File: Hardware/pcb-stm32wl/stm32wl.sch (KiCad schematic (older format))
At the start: 44 parts, among them J1 S1001-46R, J2 JST-PH, J3 S1001-46R, J4 RF_Shield_One_Piece, J5 S1001-46R, J6 S1001-46R, Q1 CEN2321A, U1 TPS22917DBV, U2 TPS3839G25, U3 TPS22917DBV, U4 RP605Z283B

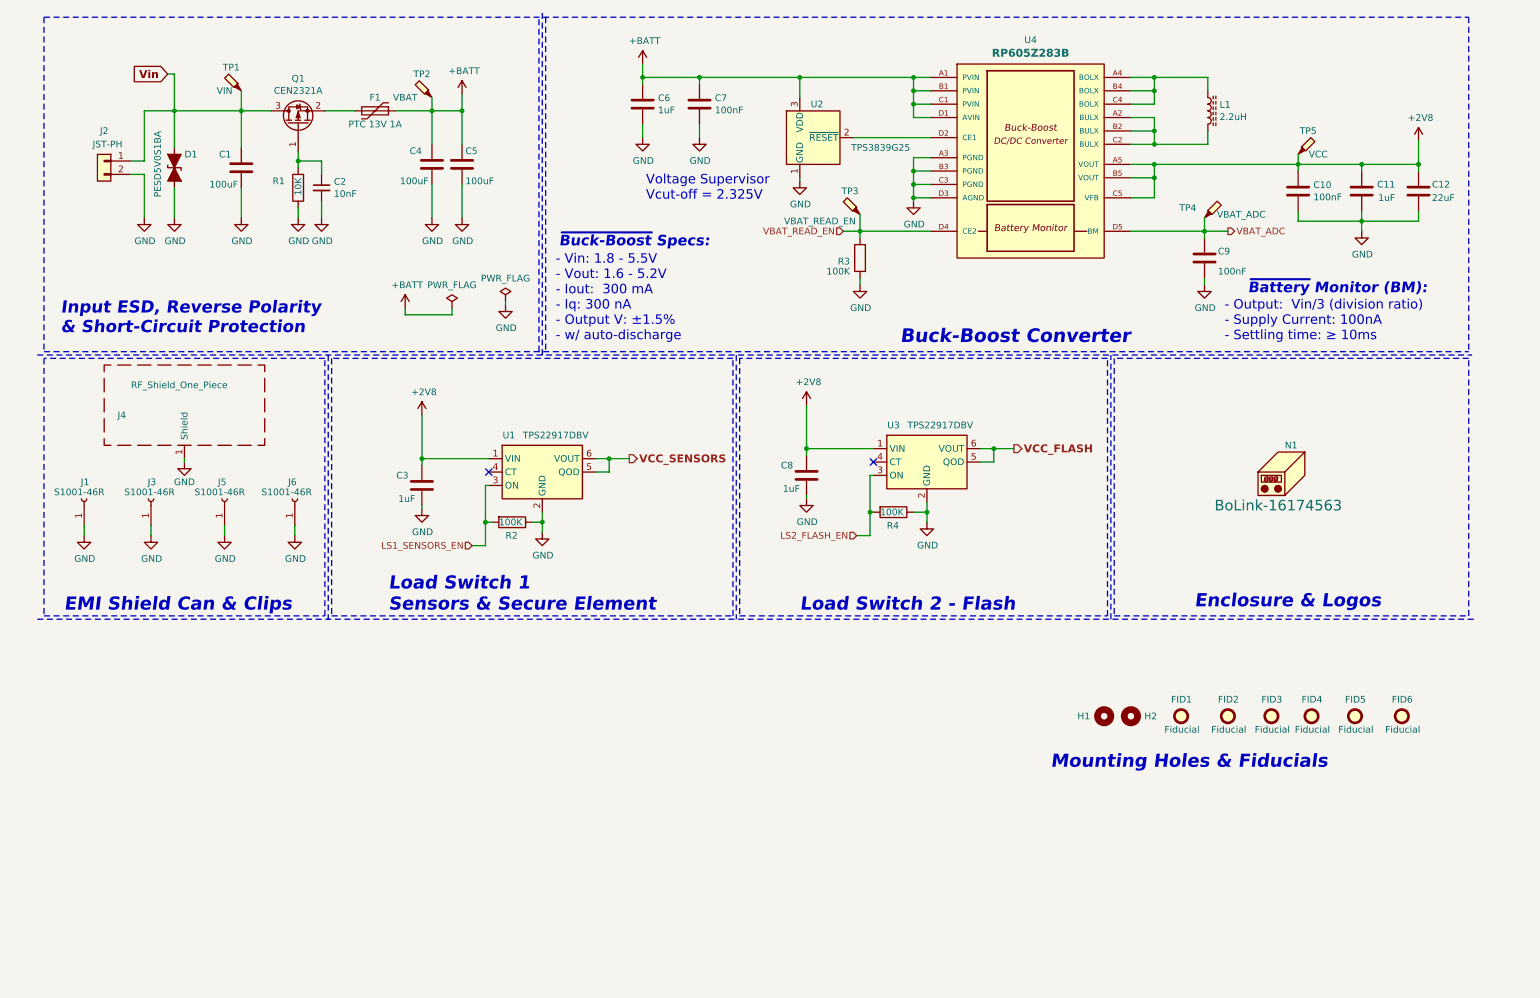
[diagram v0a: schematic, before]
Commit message: pcb,sch: Add V0.2 HW design with external battery holder
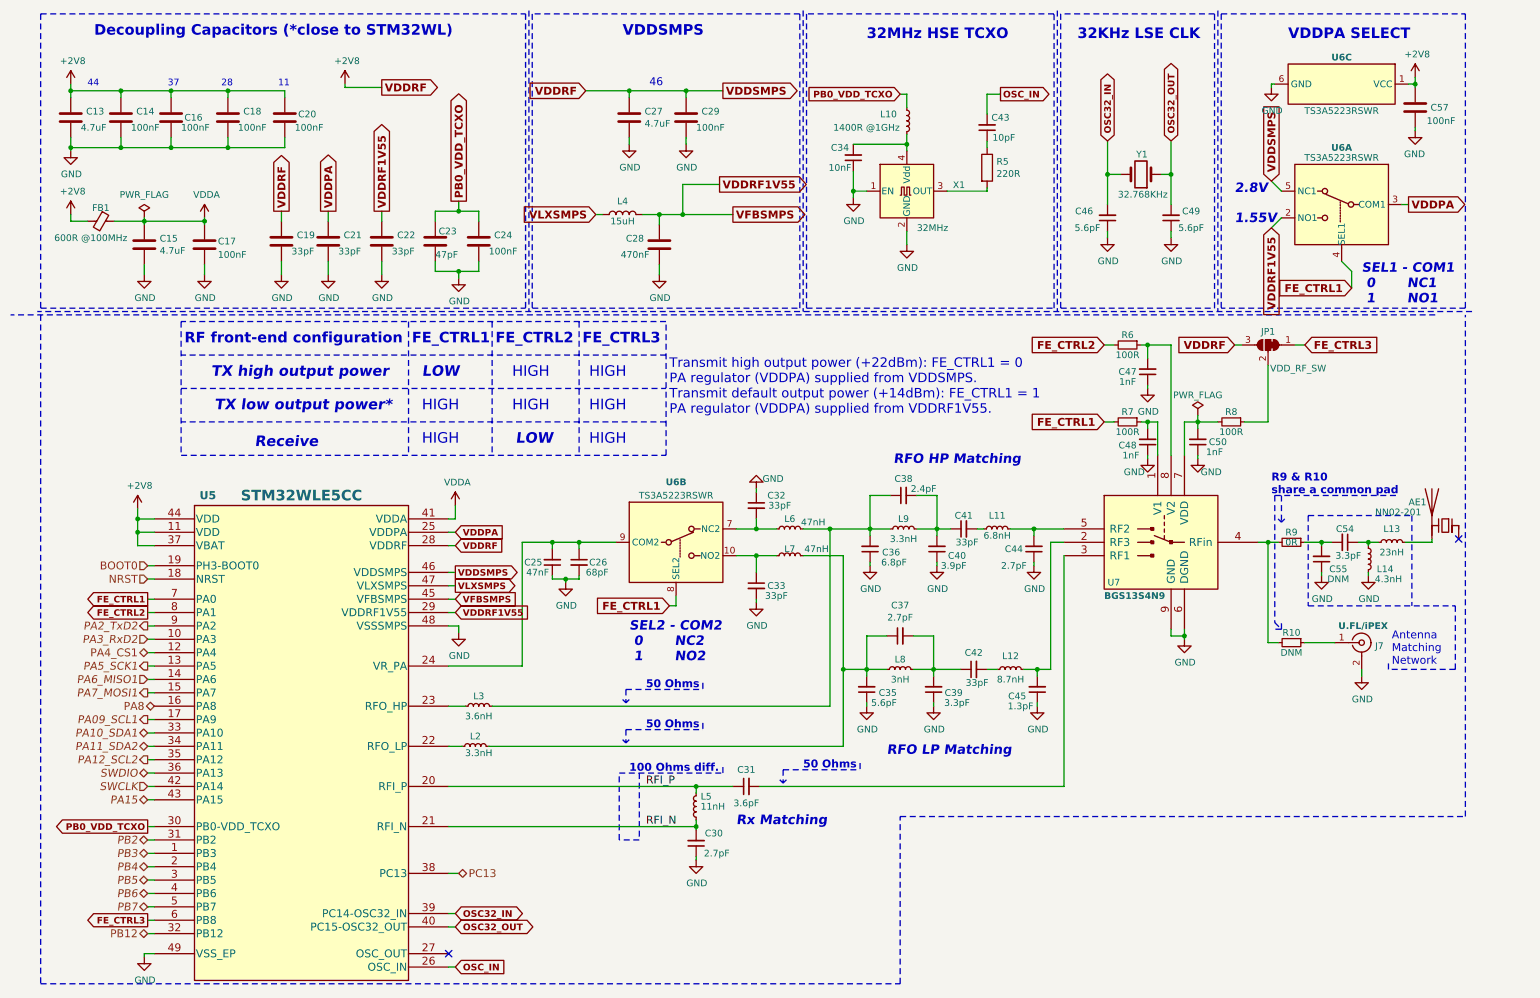
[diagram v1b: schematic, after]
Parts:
- removed C1, C4, C5: 100uF, Capacitor_SMD:C_1206_3216Metric, symbol Device:C
- removed C10, C7, C9: 100nF, Capacitor_SMD:C_0402_1005Metric, symbol Device:C
- removed C11, C3, C6, C8: 1uF, Capacitor_SMD:C_0402_1005Metric, symbol Device:C
- removed C12: 22uF, Capacitor_SMD:C_0603_1608Metric, symbol Device:C
- removed C2: 10nF, Capacitor_SMD:C_0402_1005Metric, symbol Device:C_Small
- removed D1: PESD5V0S1BA, Diode_SMD:D_SOD-323, symbol Device:D_TVS_ALT
- removed F1: PTC 13V 1A, Fuse:Fuse_1210_3225Metric_Castellated, symbol Device:Polyfuse
- removed FID1, FID2, FID3, FID4, FID5, FID6: Fiducial, Fiducial:Fiducial_0.5mm_Mask1.5mm, symbol Mechanical:Fiducial
- removed H1, H2: MountingHole, MountingHole:MountingHole_2.5mm, symbol Mechanical:MountingHole
- removed J1, J3, J5, J6: S1001-46R, node-lib-v1:RF_Shield_Clip_S1001-46R, symbol Connector:Conn_01x01_Female
- removed J2: JST-PH, Connector_JST:JST_PH_B2B-PH-SM4-TB_1x02-1MP_P2.00mm_Vertical, symbol Connector_Generic:Conn_01x02
- removed J4: RF_Shield_One_Piece, node-lib-v1:RF_Shield_SnapOn_30x20mm_w_Cutout_n_GND_Pads, symbol Device:RF_Shield_One_Piece
- removed L1: 2.2uH, node-lib-v1:L_HPC4012TF-2R2M, symbol Device:L_Core_Ferrite
- removed N1: BoLink-16174563, node-lib-v1:BoLink_704025, symbol Mechanical:Housing
- removed Q1: CEN2321A, Package_TO_SOT_SMD:SOT-23, symbol Device:Q_PMOS_GSD
- removed R1: 10K, Resistor_SMD:R_0402_1005Metric, symbol Device:R
- removed R2, R3, R4: 100K, Resistor_SMD:R_0402_1005Metric, symbol Device:R
- removed TP1: VIN, TestPoint:TestPoint_Pad_D1.5mm, symbol Connector:TestPoint_Probe
- removed TP2: VBAT, TestPoint:TestPoint_Pad_D1.5mm, symbol Connector:TestPoint_Probe
- removed TP3: VBAT_READ_EN, TestPoint:TestPoint_Pad_D1.5mm, symbol Connector:TestPoint_Probe
- removed TP4: VBAT_ADC, TestPoint:TestPoint_Pad_D1.5mm, symbol Connector:TestPoint_Probe
- removed TP5: VCC, TestPoint:TestPoint_Pad_D1.5mm, symbol Connector:TestPoint_Probe
- removed U1, U3: TPS22917DBV, Package_TO_SOT_SMD:SOT-23-6, symbol Power_Management:TPS22917DBV
- removed U2: TPS3839G25, Package_TO_SOT_SMD:SOT-23, symbol Power_Supervisor:TPS3839DBZ
- removed U4: RP605Z283B, node-lib-v1:WLCSP-20-P3_1.994x1.609mm_Layout5x4_P0.4mm, symbol node-lib-v1:RP605Zx
- added AE1: NN02-201, node-lib-v1:Antenna_Fractus_NN02-201, symbol Device:Antenna_Chip
- added C13, C15, C27: 4.7uF, Capacitor_SMD:C_0603_1608Metric, symbol Device:C
- added C14, C16, C17, C18, C20, C24, C29, C57: 100nF, Capacitor_SMD:C_0402_1005Metric, symbol Device:C
- added C19, C21, C22: 33pF, Capacitor_SMD:C_0402_1005Metric, symbol Device:C
- added C23: 47pF, Capacitor_SMD:C_0402_1005Metric, symbol Device:C
- added C25: 47nF, Capacitor_SMD:C_0402_1005Metric, symbol Device:C_Small
- added C26: 68pF, Capacitor_SMD:C_0402_1005Metric, symbol Device:C_Small
- added C28: 470nF, Capacitor_SMD:C_0603_1608Metric, symbol Device:C
- added C30, C37, C44: 2.7pF, Capacitor_SMD:C_0402_1005Metric, symbol Device:C_Small
- added C31: 3.6pF, Capacitor_SMD:C_0402_1005Metric, symbol Device:C_Small
- added C32, C33, C41, C42: 33pF, Capacitor_SMD:C_0402_1005Metric, symbol Device:C_Small
- added C34: 10nF, Capacitor_SMD:C_0402_1005Metric, symbol Device:C_Small
- added C35, C46, C49: 5.6pF, Capacitor_SMD:C_0402_1005Metric, symbol Device:C_Small
- added C36: 6.8pF, Capacitor_SMD:C_0402_1005Metric, symbol Device:C_Small
- added C38: 2.4pF, Capacitor_SMD:C_0402_1005Metric, symbol Device:C_Small
- added C39, C54: 3.3pF, Capacitor_SMD:C_0402_1005Metric, symbol Device:C_Small
- added C40: 3.9pF, Capacitor_SMD:C_0402_1005Metric, symbol Device:C_Small
- added C43: 10pF, Capacitor_SMD:C_0402_1005Metric, symbol Device:C_Small
- added C45: 1.3pF, Capacitor_SMD:C_0402_1005Metric, symbol Device:C_Small
- added C47, C48, C50: 1nF, Capacitor_SMD:C_0402_1005Metric, symbol Device:C_Small
- added C55: DNM, Capacitor_SMD:C_0402_1005Metric, symbol Device:C_Small
- added FB1: 600R @100MHz, Inductor_SMD:L_0603_1608Metric, symbol Device:Ferrite_Bead_Small
- added J7: U.FL/iPEX, Connector_Coaxial:U.FL_Hirose_U.FL-R-SMT-1_Vertical, symbol Connector:Conn_Coaxial
- added JP1: VDD_RF_SW, Jumper:SolderJumper-3_P1.3mm_Bridged12_RoundedPad1.0x1.5mm_NumberLabels, symbol Jumper:SolderJumper_3_Bridged12
- added L10: 1400R @1GHz, Inductor_SMD:L_0402_1005Metric, symbol Device:L_Small
- added L11: 6.8nH, Inductor_SMD:L_0402_1005Metric, symbol Device:L_Small
- added L12: 8.7nH, Inductor_SMD:L_0402_1005Metric, symbol Device:L_Small
- added L13: 23nH, Inductor_SMD:L_0402_1005Metric, symbol Device:L_Small
- added L14: 4.3nH, Inductor_SMD:L_0402_1005Metric, symbol Device:L_Small
- added L2, L9: 3.3nH, Inductor_SMD:L_0402_1005Metric, symbol Device:L_Small
- added L3: 3.6nH, Inductor_SMD:L_0402_1005Metric, symbol Device:L_Small
- added L4: 15uH, node-lib-v1:L_0805_2012Metric_custom, symbol Device:L
- added L5: 11nH, Inductor_SMD:L_0402_1005Metric, symbol Device:L_Small
- added L6, L7: 47nH, Inductor_SMD:L_0402_1005Metric, symbol Device:L_Small
- added L8: 3nH, Inductor_SMD:L_0402_1005Metric, symbol Device:L_Small
- added R10: DNM, Resistor_SMD:R_0402_1005Metric, symbol Device:R_Small
- added R5: 220R, Inductor_SMD:L_0402_1005Metric, symbol Device:R
- added R6, R7, R8: 100R, Resistor_SMD:R_0402_1005Metric, symbol Device:R_Small
- added R9: 0R, Resistor_SMD:R_0402_1005Metric, symbol Device:R_Small
- added U5: STM32WLE5CC, Package_DFN_QFN:QFN-48-1EP_7x7mm_P0.5mm_EP5.45x5.45mm, symbol node-lib-v1:STM32WLxx_QFN48
- added U6: TS3A5223RSWR, Package_DFN_QFN:UQFN-10_1.4x1.8mm_P0.4mm, symbol node-lib-v1:TS3A5223RSWR
- added U7: BGS13S4N9, node-lib-v1:RFSW_BGS13S4N9E6327XTSA1, symbol node-lib-v1:BGS13S4N9
- added X1: 32MHz, Crystal:Crystal_SMD_Abracon_ABM10-4Pin_2.5x2.0mm, symbol node-lib-v1:TCXO-xxxMHz
- added Y1: 32.768KHz, node-lib-v1:Crystal_SMD_NX2012SA_32.768KHz, symbol Device:Crystal
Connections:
- net +2V8: now also C13.1, C14.1, C16.1, C18.1, C19.1, C20.1, C27.1, C29.1, C57.1, FB1.2, JP1.3 (B), U5.11 (VDD), U5.28 (VDDRF), U5.37 (VBAT), U5.44 (VDD), U5.46 (VDDSMPS), U6.1 (VCC), U6.5 (NC1)
- net GND: now also C13.2, C14.2, C15.2, C16.2, C17.2, C18.2, C19.2, C20.2, C21.2, C22.2, C23.2, C24.2, C25.1, C26.2, C27.2, C28.2, C29.2, C30.1, C32.1, C33.2, C34.1, C35.1, C36.1, C39.1, C40.1, C44.1, C45.1, C46.1, C47.1, C48.1, C49.1, C50.1, C55.1, C57.2, J7.2 (Ext), L14.1, U5.48 (VSSSMPS), U5.49 (VSS_EP), U6.6 (GND), U7.6 (DGND), U7.9 (GND), X1.1 (EN), X1.2 (GND)
- new net: L2.1, U5.22 (RFO_LP)
- new net: L3.1, U5.23 (RFO_HP)
- new net: C25.2, C26.1, U5.24 (VR_PA), U6.9 (COM2)
- new net: C36.2, C38.1, L3.2, L6.2, L9.1
- new net: C35.2, C37.1, L2.2, L7.2, L8.1
- new net: C31.2, U7.3 (RF1)
- new net: C48.2, R7.1, U7.1 (V1)
- new net: C45.2, L12.2, U7.2 (RF3)
- new net: R10.2, R9.2, U7.4 (RFin)
- new net: C44.2, L11.2, U7.5 (RF2)
- new net: C50.2, R8.2, U7.7 (VDD)
- new net: C47.2, R6.1, U7.8 (V2)
- new net: J7.1 (In), R10.1
- new net: C54.2, C55.2, R9.1
- new net: JP1.2 (C), R8.1
- new net: C32.2, L6.1, U6.7 (NC2)
- new net: C33.1, L7.1, U6.10 (NO2)
- new net: C37.2, C39.2, C42.1, L8.2
- new net: C42.2, L12.1
- new net: C38.2, C40.2, C41.1, L9.2
- new net: C41.2, L11.1
- new net: C43.1, R5.1
- new net: R5.2, X1.3 (OUT)
- new net: C34.2, L10.2, X1.4 (Vdd)
- new net: C54.1, L13.1, L14.2
- new net: AE1.2 (PCB_Trace), L13.2
- new net BOOT0: U5.19 (PH3-BOOT0)
- new net FE_CTRL1: R7.2, U5.7 (PA0), U6.4 (SEL1), U6.8 (SEL2)
- new net FE_CTRL2: R6.2, U5.8 (PA1)
- new net FE_CTRL3: JP1.1 (A), U5.6 (PB8)
- new net NRST: U5.18 (NRST)
- new net OSC32_IN: C46.2, U5.39 (PC14-OSC32_IN), Y1.2
- new net OSC32_OUT: C49.2, U5.40 (PC15-OSC32_OUT), Y1.1
- new net OSC_IN: C43.2, U5.26 (OSC_IN)
- new net PA09_SCL1: U5.17 (PA9)
- new net PA10_SDA1: U5.33 (PA10)
- new net PA11_SDA2: U5.34 (PA11)
- new net PA12_SCL2: U5.35 (PA12)
- new net PA15: U5.43 (PA15)
- new net PA2_TxD2: U5.9 (PA2)
- new net PA3_RxD2: U5.10 (PA3)
- new net PA4_CS1: U5.12 (PA4)
- new net PA5_SCK1: U5.13 (PA5)
- new net PA6_MISO1: U5.14 (PA6)
- new net PA7_MOSI1: U5.15 (PA7)
- new net PA8: U5.16 (PA8)
- new net PB0_VDD_TCXO: C23.1, C24.1, L10.1, U5.30 (PB0-VDD_TCXO)
- new net PB12: U5.32 (PB12)
- new net PB2: U5.31 (PB2)
- new net PB3: U5.1 (PB3)
- new net PB4: U5.2 (PB4)
- new net PB5: U5.3 (PB5)
- new net PB6: U5.4 (PB6)
- new net PB7: U5.5 (PB7)
- new net PC13: U5.38 (PC13)
- new net RFI_N: C30.2, L5.1, U5.21 (RFI_N)
- new net RFI_P: C31.1, L5.2, U5.20 (RFI_P)
- new net SWCLK: U5.42 (PA14)
- new net SWDIO: U5.36 (PA13)
- new net VDDA: C15.1, C17.1, FB1.1, U5.41 (VDDA)
- new net VDDPA: C21.1, U5.25 (VDDPA), U6.3 (COM1)
- new net VDDRF1V55: C22.1, C28.1, L4.2, U5.29 (VDDRF1V55), U5.45 (VFBSMPS), U6.2 (NO1)
- new net VLXSMPS: L4.1, U5.47 (VLXSMPS)
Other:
- note added: "1.55V"
- note added: "100 Ohms diff."
- note added: "11"
- note added: "2.8V"
- note added: "28"
- note added: "32KHz LSE CLK"
- note added: "32MHz HSE TCXO"
- note added: "37"
- note added: "44"
- note added: "46"
- note added: "50 Ohms"
- note added: "Antenna\nMatching\nNetwork"
- note added: "Decoupling Capacitors (*close to STM32WL)"
- note added: "FE_CTRL1"
- note added: "FE_CTRL2"
- note added: "FE_CTRL3"
- note added: "HIGH"
- note added: "LOW"
- note added: "R9 & R10\nshare a common pad"
- note added: "RF front-end configuration"
- note added: "RFO HP Matching"
- note added: "RFO LP Matching"
- note added: "Receive"
- note added: "Rx Matching"
- note added: "SEL1 - COM1\n 0 NC1\n 1 NO1"
- note added: "SEL2 - COM2\n 0 NC2\n 1 NO2"
- note added: "TX high output power"
- note added: "TX low output power*"
- note added: "Transmit high output power (+22dBm): FE_CTRL1 = 0\nPA regulator (VDDPA) supplied from VDDSMPS.\nTransmit default output power (+14dBm): FE_CTRL1 = 1\nPA regulator (VDDPA) supplied from VDDRF1V55."
- note added: "VDDPA SELECT"
- note added: "VDDSMPS"
- note removed: "- Output: Vin/3 (division ratio)\n- Supply Current: 100nA\n- Settling time: ≥ 10ms"
- note removed: "- Vin: 1.8 - 5.5V\n- Vout: 1.6 - 5.2V\n- Iout: 300 mA\n- Iq: 300 nA\n- Output V: ±1.5%\n- w/ auto-discharge"
- note removed: "Buck-Boost Converter"
- note removed: "EMI Shield Can & Clips"
- note removed: "Enclosure & Logos"
- note removed: "Input ESD, Reverse Polarity \n& Short-Circuit Protection"
- note removed: "Load Switch 1 \nSensors & Secure Element"
- note removed: "Load Switch 2 - Flash"
- note removed: "Mounting Holes & Fiducials"
- note removed: "Voltage Supervisor\nVcut-off = 2.325V"
- note removed: "~Battery Monitor (BM):"
- note removed: "~Buck-Boost Specs:"

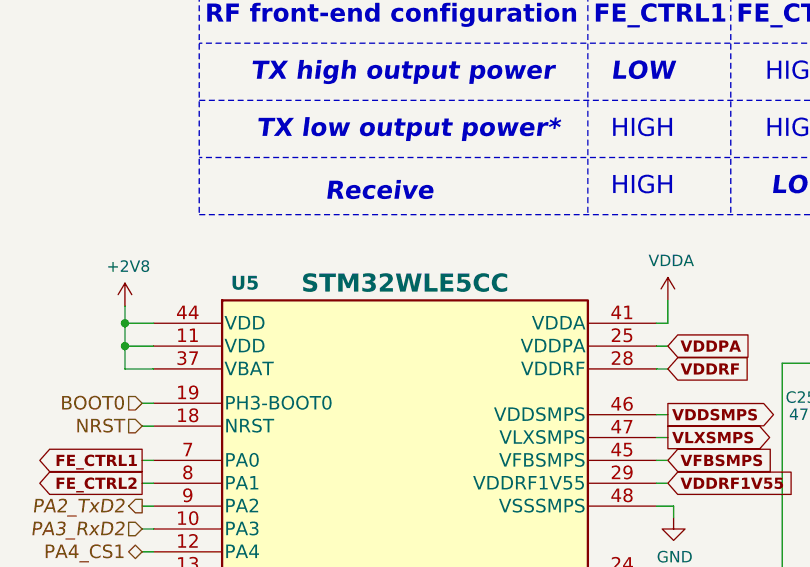
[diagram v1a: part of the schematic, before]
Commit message: sch, doc: Adding updated BOM files
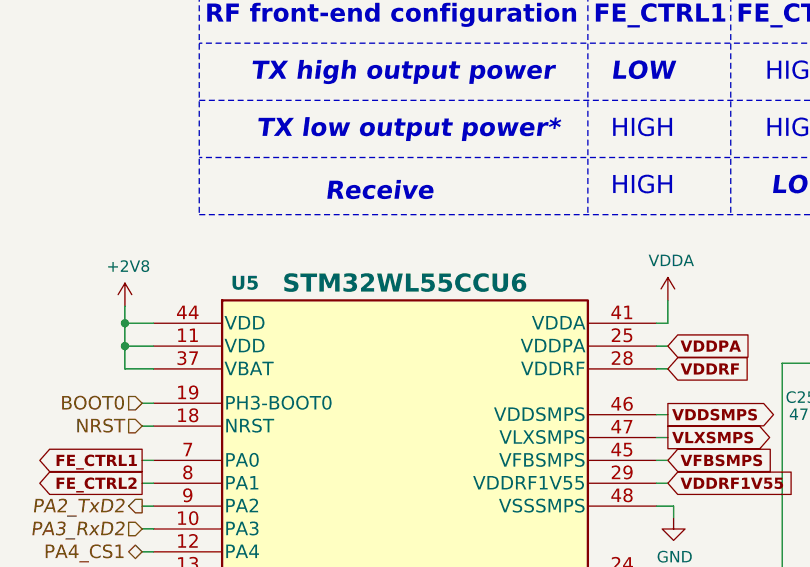
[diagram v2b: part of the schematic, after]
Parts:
- U5: value STM32WLE5CC -> STM32WL55CCU6; URL https://www.st.com/content/st_com/en/products/microcontroll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 -> https://www.st.com/en/microcontrollers-microprocessors/stm3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
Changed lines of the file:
@@
 P 1650 4175
 F 0 "U5" H 1750 4250 60  0000 C CNB
-F 1 "STM32WLE5CC" H 2450 4250 79  0000 C CNB
+F 1 "STM32WL55CCU6" H 2450 4250 79  0000 C CNB
 F 2 "Package_DFN_QFN:QFN-48-1EP_7x7mm_P0.5mm_EP5.45x5.45mm" H 2450 1775 60  0001 C CNN
-F 3 "https://www.st.com/resource/en/datasheet/stm32wle5jc.pdf" H 1350 3475 60  0001 C CNN
+F 3 "https://www.st.com/resource/en/datasheet/stm32wl55cc.pdf" H 1350 3475 60  0001 C CNN
 F 4 "STM32WLE5CCU6" H 1650 4175 50  0001 C CNN "MPN"
-F 5 "https://www.st.com/content/st_com/en/products/microcontrollers-microprocessors/stm32-32-bit-arm-cortex-mcus/stm32-wireless-mcus/stm32wl-series/stm32wlex/stm32wle5cc.html#sample-buy" H 1650 4175 50  0001 C CNN "URL"
+F 5 "https://www.st.com/en/microcontrollers-microprocessors/stm32wl55cc.html" H 1650 4175 50  0001 C CNN "URL"
 	1    1650 4175
 	1    0    0    -1
